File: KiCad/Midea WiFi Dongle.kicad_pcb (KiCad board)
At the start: 2 copper layers, 23 x 41 mm, 21 parts, among them J1 USB_A, Q1 BSS138, Q2 BSS138, SW1 SW_Push, SW2 SW_Push, U1 AMS1117-3.3, U2 WT0132C6-S5

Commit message: Added BMP (for traditional, toner, paper, iron method) and STL (negative, for 3D printer method, with spray paint, requires 0.25mm nozzle)
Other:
- board text added: "Design by Sascha Puligheddu (2025)"
- board text added: "Midea Dongle mono-sheet"
- board text removed: "Midea WiFi Dongle v3 mono-sheet"
- board text removed: "Original Design by René Klootwijk (2020)"
- board text removed: "v2 Changes by Sascha (2025)"
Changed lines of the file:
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@@
 		(tenting front back)
 		(pcbplotparams
-			(layerselection 0x00000000_00000000_55555555_5755f5ff)
+			(layerselection 0x00000000_00000000_55555555_57555551)
 			(plot_on_all_layers_selection 0x00000000_00000000_00000000_00000000)
 			(disableapertmacros no)
@@
 		(layer "Edge.Cuts")
 	)
-	(gr_text "Original Design by\nRené Klootwijk (2020)"
+	(gr_text "Design by\nSascha Puligheddu (2025)"
 		(at 153.9 97.4075 0)
 		(layer "B.SilkS")
@@
 		)
 	)
-	(gr_text "Midea WiFi Dongle v3 mono-sheet"
+	(gr_text "Midea Dongle mono-sheet"
 		(at 153.9 94 0)
 		(layer "B.SilkS")
@@
 		)
 	)
-	(gr_text "v2 Changes by Sascha (2025)"
-		(at 153.9 101.15 0)
-		(layer "B.SilkS")
-		(effects
-			(font
-				(size 0.8 0.8)
-				(thickness 0.1524)
-			)
-			(justify mirror)
-		)
-	)
 	(gr_text "10k"
 		(at 163.1 107.9 0)
@@
 	)
 	(segment
-		(start 158.4 115.3975)
-		(end 158.4 118.05)
+		(start 158.4 118.05)
+		(end 157.4 119.05)
 		(width 0.4)
 		(layer "F.Cu")
@@
 	)
 	(segment
-		(start 158.4 118.05)
-		(end 157.4 119.05)
+		(start 158.4 115.3975)
+		(end 158.4 118.05)
 		(width 0.4)
 		(layer "F.Cu")

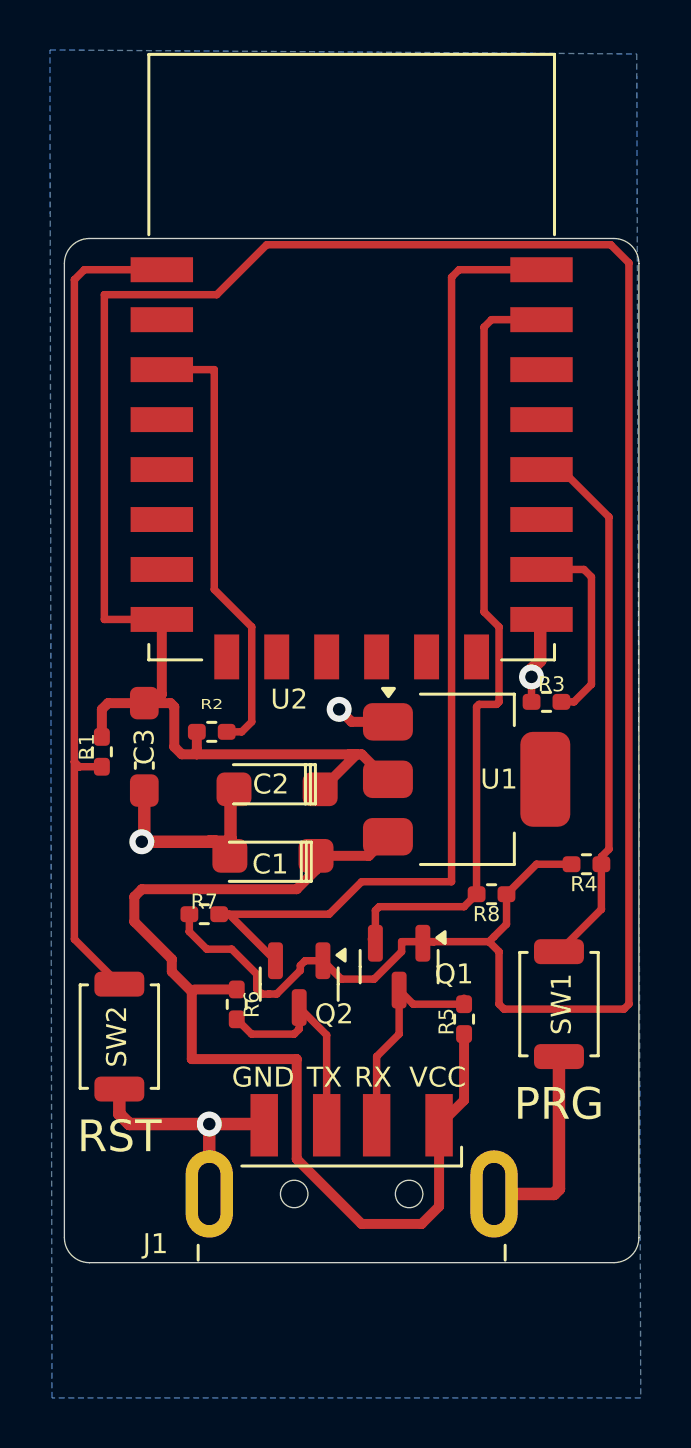
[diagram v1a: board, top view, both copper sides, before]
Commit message: updated 3D model, I have to update the 3D printing model too.
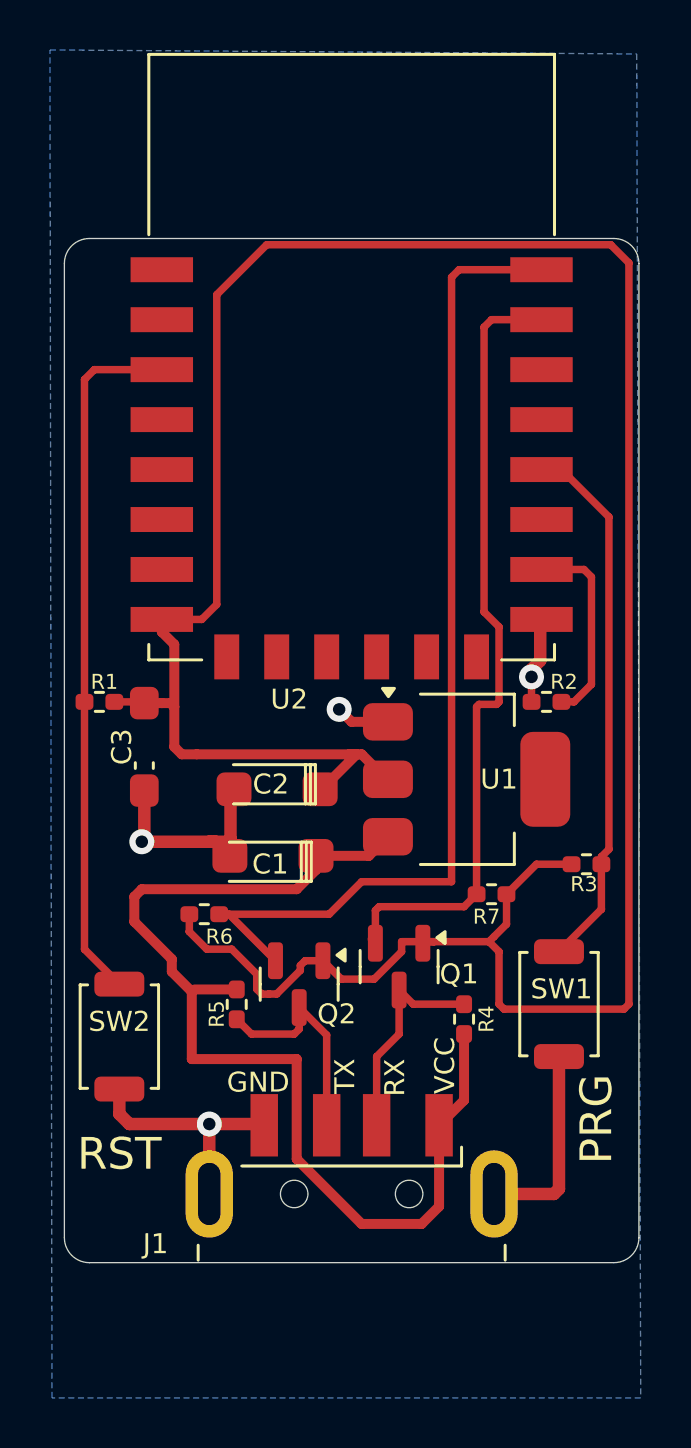
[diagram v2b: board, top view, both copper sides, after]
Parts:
- removed the R2 at (148.3, 103.3)
- moved R1 2.00 mm to (143.8, 102.1), turned to 0 degrees
- renumbered R3 to R2, R4 to R3, R5 to R4, R6 to R5, R7 to R6, R8 to R7
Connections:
- R1 pad 1: /RESET -> /EN
- SW2 pad 2: /RESET -> /EN
- U2 pad 1: /RESET -> unconnected-(U2-GPIO0-Pad1)
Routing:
- net /RESET: track 33.8 -> 0.00 mm
- net /EN: track 18.8 -> 28.0 mm
- net +3V3: track 118.3 -> 110.6 mm
- net /GPIO9: track 21.8 -> 21.0 mm
